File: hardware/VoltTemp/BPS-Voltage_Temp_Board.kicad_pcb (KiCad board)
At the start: 2 copper layers, 98.2 x 56.2 mm, 144 parts, among them IC1 ISO1641BDR, J10 53307-2471, J11 Conn_01x07, J12 Conn_01x04, J13 Conn_01x04, J5 Logic_Analyzer, J6 Conn_01x04, J7 Conn_01x04, J8 Conn_01x06, J9 Conn_01x03, SW1 BOOT, U1 EL3H7, U12 TLV9062xD, U13 TLV9062xD, U14 TLV9062xD, U2 BQ7692003PW, U3 EL3H7, U4 TLV9062xD, U6 TLV9062xD

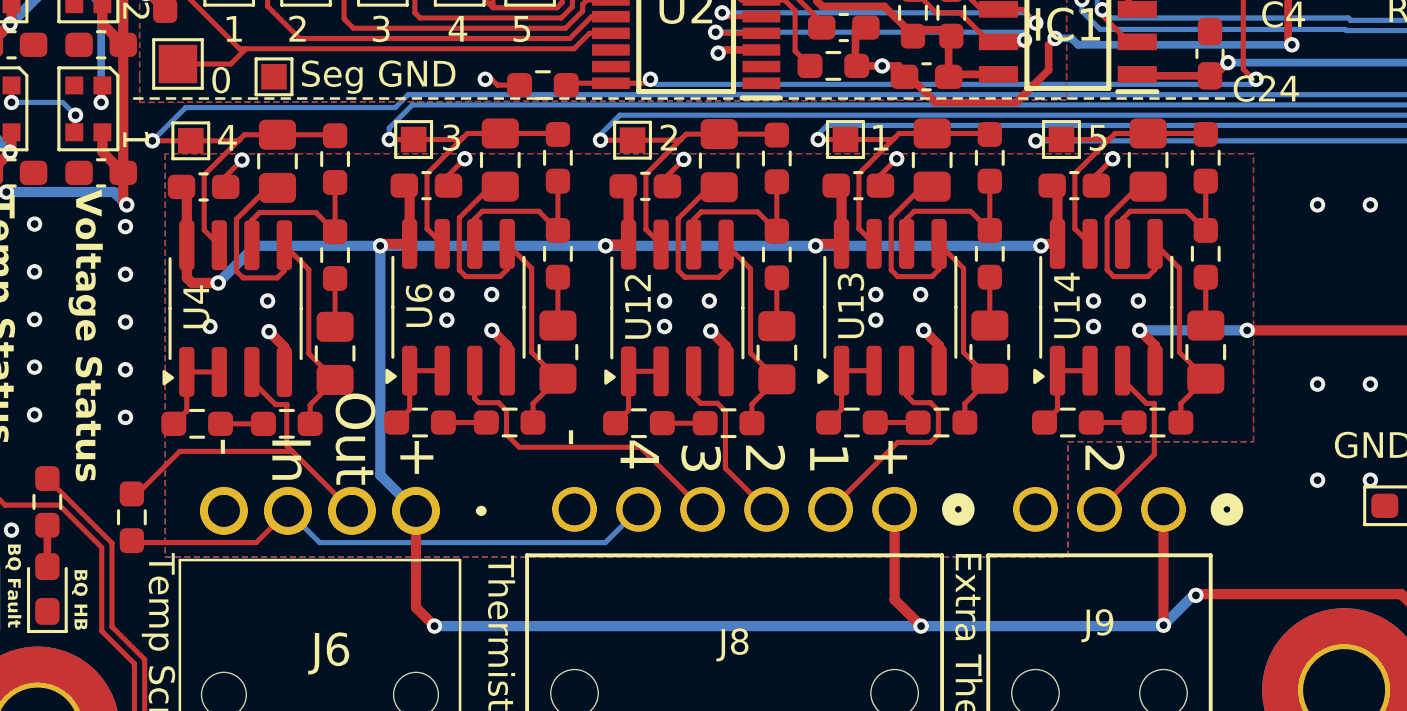
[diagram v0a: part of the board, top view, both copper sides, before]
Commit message: change 4.7pF cap to 470pF
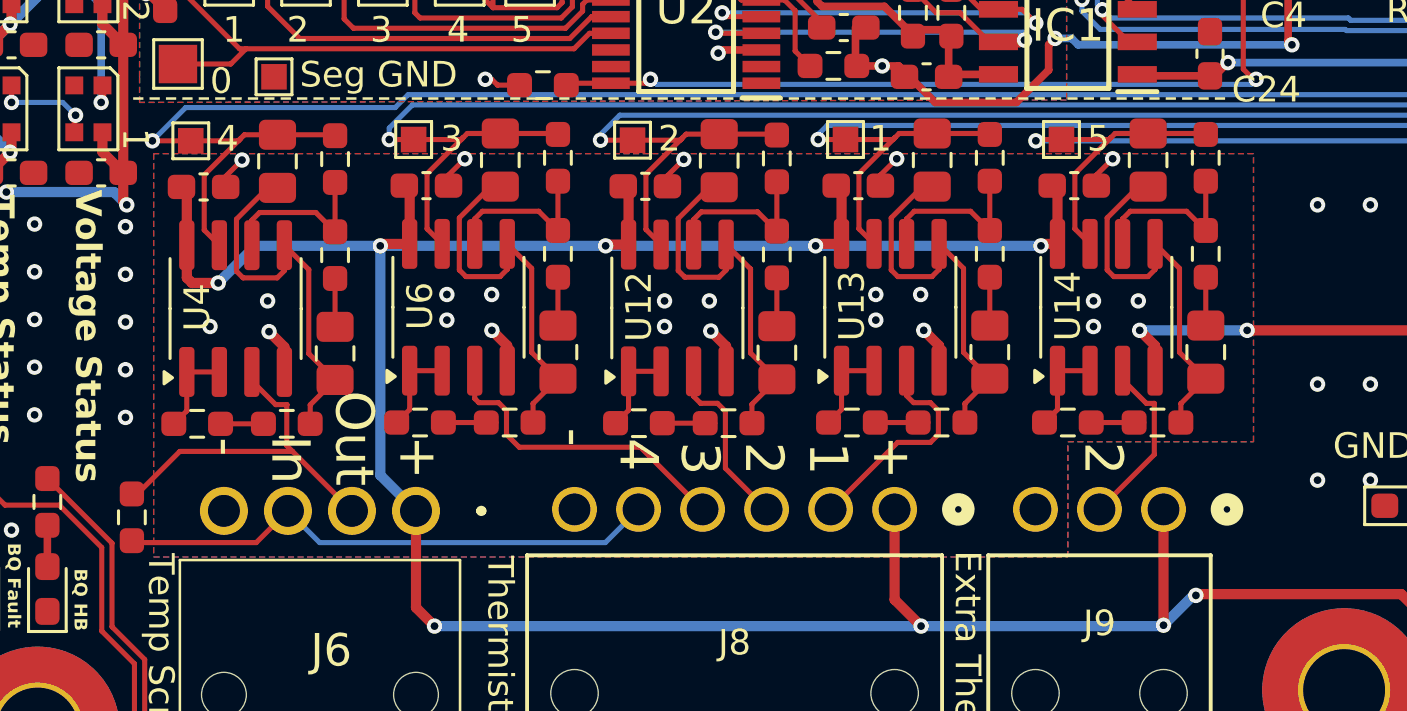
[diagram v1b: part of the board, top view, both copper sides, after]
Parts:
- C4: value 4.7pF -> 470pF
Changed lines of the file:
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@@
 			)
 		)
-		(property "Value" "4.7pF"
+		(property "Value" "470pF"
 			(at 0 1.43 90)
 			(layer "F.Fab")
@@
 			)
 		)
-		(property "P/N" "C0603C479J5GACAUTO"
+		(property "P/N" "06033C471K4Z2A"
 			(at 0 0 270)
 			(unlocked yes)
@@
 		(polygon
 			(pts
-				(xy 162.25 111.75) (xy 162.25 107.25) (xy 169.5 107.25) (xy 169.5 96) (xy 127 96) (xy 127 111.75)
+				(xy 162.25 111.75) (xy 162.25 107.25) (xy 169.5 107.25) (xy 169.5 96) (xy 126.55 96) (xy 126.55 111.75)
 			)
 		)

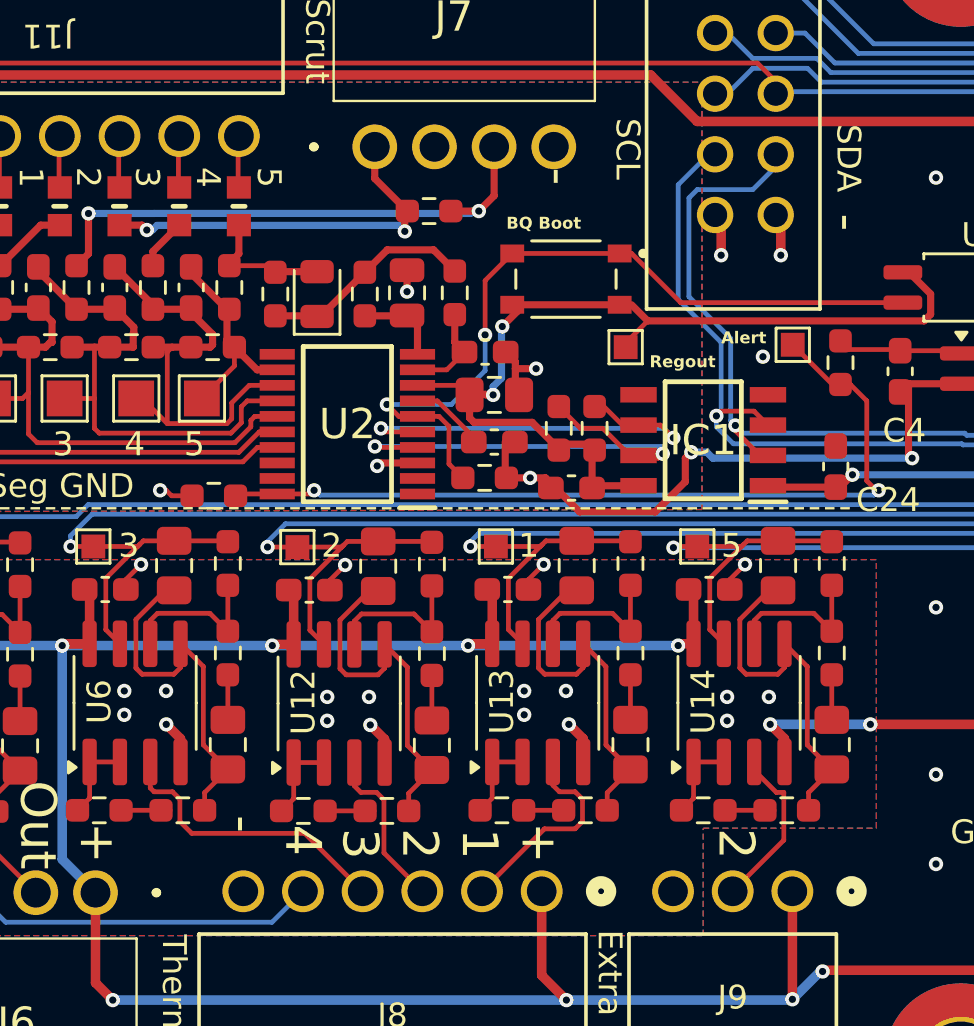
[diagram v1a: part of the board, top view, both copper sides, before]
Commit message: update connector silkscreen
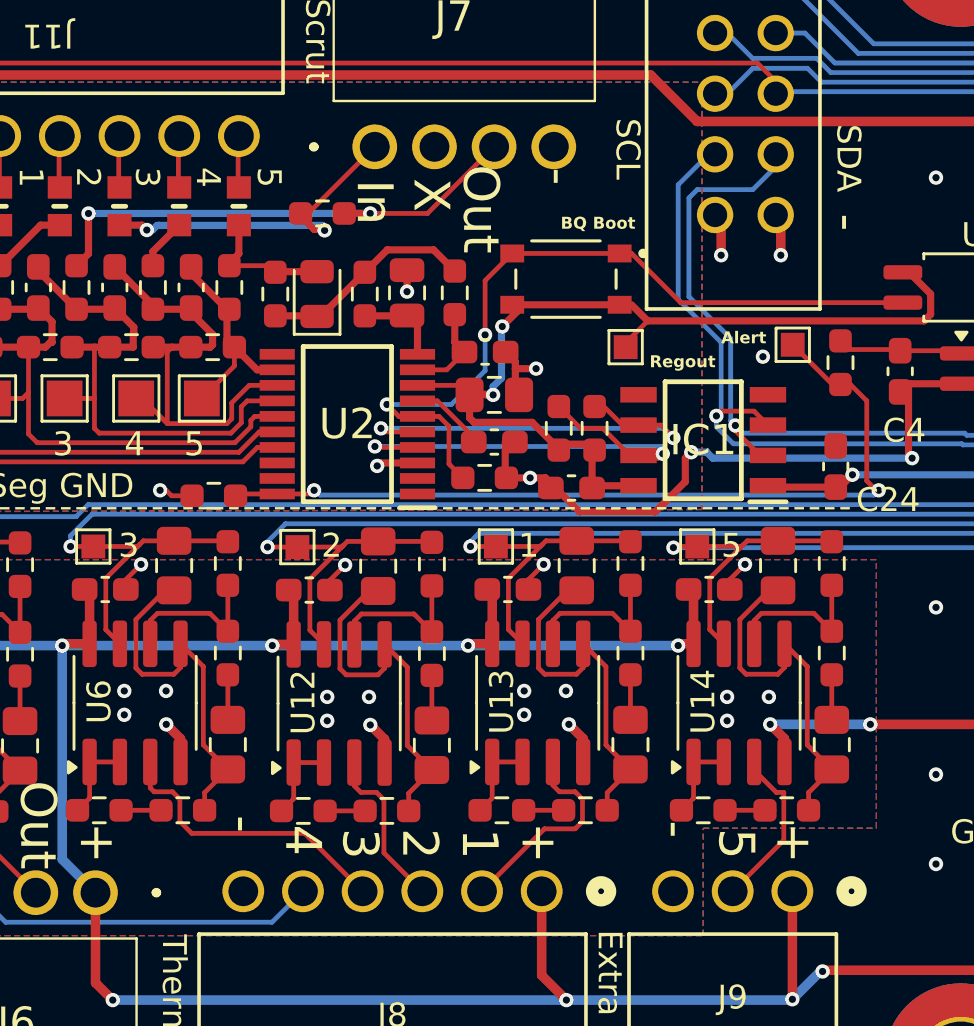
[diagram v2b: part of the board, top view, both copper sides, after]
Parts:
- moved R23 4.47 mm to (146.3, 81.5)
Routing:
- net /VoltageConn/3&4COM: track 16.4 -> 14.5 mm
- net /VoltageConn/3&4COM_Out: track 22.9 -> 21.7 mm
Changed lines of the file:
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@@
 	(footprint "Resistor_SMD:R_0603_1608Metric_Pad0.98x0.95mm_HandSolder"
 		(layer "F.Cu")
-		(at 150.7676 81.4)
+		(at 146.3 81.5)
 		(descr "Resistor SMD 0603 (1608 Metric), square (rectangular) end terminal, IPC_7351 nominal with elongated pad for handsoldering. (Body size source: IPC-SM-782 page 72, https://www.pcb-3d.com/wordpress/wp-content/uploads/ipc-sm-782a_amendment_1_and_2.pdf), generated with kicad-footprint-generator")
 		(tags "resistor handsolder")
@@
 	)
 	(gr_text "BQ Boot"
-		(at 154 82.2 0)
+		(at 156.275 82.2 0)
 		(layer "F.SilkS" knockout)
 		(effects
@@
 		)
 	)
+	(gr_text "In"
+		(at 147.6 80.075 270)
+		(layer "F.SilkS")
+		(effects
+			(font
+				(size 1.5 1.5)
+				(thickness 0.1)
+			)
+			(justify left bottom)
+		)
+	)
 	(gr_text "+"
 		(at 136 107 270)
@@
 		)
 	)
+	(gr_text "+"
+		(at 165.175 107 270)
+		(layer "F.SilkS")
+		(effects
+			(font
+				(size 1.5 1.5)
+				(thickness 0.1)
+			)
+			(justify left bottom)
+		)
+	)
 	(gr_text "5"
 		(at 140.5 91.75 0)
@@
 		)
 	)
-	(gr_text "2"
+	(gr_text "5"
 		(at 162.75 107.25 270)
 		(layer "F.SilkS")
@@
 		)
 	)
+	(gr_text "X"
+		(at 149.975 80.025 270)
+		(layer "F.SilkS")
+		(effects
+			(font
+				(size 1.5 1.5)
+				(thickness 0.1)
+			)
+			(justify left bottom)
+		)
+	)
+	(gr_text "-"
+		(at 160.225 106.925 270)
+		(layer "F.SilkS")
+		(effects
+			(font
+				(size 1.5 1.5)
+				(thickness 0.1)
+			)
+			(justify left bottom)
+		)
+	)
 	(gr_text "SDA"
 		(at 167.75 77.75 270)
@@
 		)
 	)
+	(gr_text "Out"
+		(at 152.05 79.45 270)
+		(layer "F.SilkS")
+		(effects
+			(font
+				(size 1.5 1.5)
+				(thickness 0.1)
+			)
+			(justify left bottom)
+		)
+	)
 	(gr_text "Extra Therm"
 		(at 157.75 111.5 270)
@@
 	)
 	(segment
+		(start 145.956097 82.168597)
+		(end 145.3875 81.6)
+		(width 0.3)
+		(layer "F.Cu")
+		(net 56)
+	)
+	(segment
 		(start 138.74 81.99)
 		(end 137.8 81.99)
@@
 	)
 	(segment
-		(start 148.491 78.708606)
-		(end 148.491 80.0359)
+		(start 146.351167 82.168597)
+		(end 145.956097 82.168597)
 		(width 0.3)
 		(layer "F.Cu")
@@
 	)
 	(segment
-		(start 148.491 80.0359)
-		(end 149.8551 81.4)
-		(width 0.3)
+		(start 145.3875 81.6)
+		(end 145.599606 81.6)
+		(width 0.2)
 		(layer "F.Cu")
 		(net 56)
 	)
 	(segment
-		(start 149.75 81.5051)
-		(end 149.8551 81.4)
-		(width 0.3)
+		(start 145.599606 81.6)
+		(end 148.491 78.708606)
+		(width 0.2)
 		(layer "F.Cu")
 		(net 56)
 	)
 	(segment
-		(start 149.75 82.25)
-		(end 149.75 81.5051)
+		(start 146.391194 82.208624)
+		(end 146.351167 82.168597)
 		(width 0.3)
 		(layer "F.Cu")
@@
 	)
 	(via
-		(at 149.75 82.25)
+		(at 146.391194 82.208624)
 		(size 0.6)
 		(drill 0.3)
@@
 	)
 	(segment
-		(start 139.176921 82.193839)
-		(end 139.37076 82)
+		(start 146.299289 82.116719)
+		(end 146.299289 82)
 		(width 0.3)
 		(layer "B.Cu")
@@
 	)
 	(segment
-		(start 138.943839 82.193839)
+		(start 139.458521 82)
+		(end 139.45752 82.001)
+		(width 0.3)
+		(layer "B.Cu")
+		(net 56)
+	)
+	(segment
+		(start 146.391194 82.208624)
+		(end 146.299289 82.116719)
+		(width 0.3)
+		(layer "B.Cu")
+		(net 56)
+	)
+	(segment
+		(start 139.36976 82.001)
 		(end 139.176921 82.193839)
 		(width 0.3)
@@
 	)
 	(segment
-		(start 149.5 82)
-		(end 149.75 82.25)
+		(start 139.45852 82)
+		(end 139.458521 82)
 		(width 0.3)
 		(layer "B.Cu")
@@
 	)
 	(segment
-		(start 139.37076 82)
-		(end 149.5 82)
+		(start 146.299289 82)
+		(end 139.45852 82)
 		(width 0.3)
 		(layer "B.Cu")
@@
 	)
 	(segment
-		(start 153.491 78.708606)
-		(end 153.491 80.759)
+		(start 139.45752 82.001)
+		(end 139.36976 82.001)
 		(width 0.3)
+		(layer "B.Cu")
+		(net 56)
+	)
+	(segment
+		(start 139.176921 82.193839)
+		(end 138.943839 82.193839)
+		(width 0.3)
+		(layer "B.Cu")
+		(net 56)
+	)
+	(segment
+		(start 150.700606 81.499)
+		(end 148.3 81.499)
+		(width 0.2)
 		(layer "F.Cu")
 		(net 57)
 	)
 	(segment
-		(start 152.85 81.4)
-		(end 151.6801 81.4)
-		(width 0.3)
+		(start 153.491 78.708606)
+		(end 150.700606 81.499)
+		(width 0.2)
 		(layer "F.Cu")
 		(net 57)
@@
 	)
 	(segment
-		(start 153.491 80.759)
-		(end 152.85 81.4)
+		(start 148.3 81.499)
+		(end 147.3135 81.499)
+		(width 0.3)
+		(layer "F.Cu")
+		(net 57)
+	)
+	(segment
+		(start 147.3135 81.499)
+		(end 147.2125 81.6)
 		(width 0.3)
 		(layer "F.Cu")
@@
 	)
 	(via
-		(at 152.85 81.4)
+		(at 148.3 81.499)
 		(size 0.6)
 		(drill 0.3)
@@
 	)
 	(segment
-		(start 152.85 81.4)
-		(end 152.6 81.4)
-		(width 0.3)
-		(layer "B.Cu")
-		(net 57)
-	)
-	(segment
 		(start 139.251 81.499)
 		(end 139.25 81.5)
@@
 	)
 	(segment
-		(start 149.707521 81.499)
+		(start 148.3 81.499)
 		(end 139.251 81.499)
 		(width 0.3)
@@
 	)
 	(segment
-		(start 152.5 81.5)
-		(end 149.708521 81.5)
-		(width 0.3)
-		(layer "B.Cu")
-		(net 57)
-	)
-	(segment
 		(start 139.25 81.5)
 		(end 136.5 81.5)
 		(width 0.3)
 		(layer "B.Cu")
-		(net 57)
-	)
-	(segment
-		(start 149.70752 81.499)
-		(end 149.707521 81.499)
-		(width 0.3)
-		(layer "B.Cu")
-		(net 57)
-	)
-	(segment
-		(start 152.6 81.4)
-		(end 152.5 81.5)
-		(width 0.3)
-		(layer "B.Cu")
-		(net 57)
-	)
-	(segment
-		(start 149.708521 81.5)
-		(end 149.70752 81.499)
-		(width 0.3)
-		(layer "B.Cu")

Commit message: update cubemx
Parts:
- moved LOGO1 4.88 mm to (196.6, 85.6)
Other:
- board text added: "Lakshay Gupta & Clark Rucker"
- board text added: "PA11"
- board text added: "PA12"
- board text added: "Todo: - Layout :( [X] - Update constrains [X] - Mirror thermistor flex pinout [X] - Label voltage connector [X] - Fix iso i2c footprint [X] - Make proper edge cuts [X] - Add stitching vias [X] - Update pcb from schematic once schematic todo done [X] - Figure out edge to connector clearance for nanofits [] - Redo addressable led routing [X] - Verify 24V traces can handle 8 Volttemps of current [X]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"
- board text removed: "Todo: - Layout :( [X] - Update constrains [X] - Mirror thermistor flex pinout [X] - Label voltage connector [] - Fix iso i2c footprint [X] - Make proper edge cuts [X] - Add stitching vias [X] - Update pcb from schematic once schematic todo done [X] - Figure out edge to connector clearance for nanofits [] - Redo addressable led routing [X] - Verify 24V traces can handle 8 Volttemps of current [X] 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"
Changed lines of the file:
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@@
 			)
 		)
+		(property "P/N" "53307-2471"
+			(at 0 0 180)
+			(unlocked yes)
+			(layer "F.Fab")
+			(hide yes)
+			(effects
+				(font
+					(size 1 1)
+					(thickness 0.15)
+				)
+			)
+		)
 		(sheetname "/")
 		(sheetfile "BPS-Voltage_Temp_Board.kicad_sch")
@@
 	(footprint "UTSVT_Logos:Hallock_Image_Small"
 		(layer "B.Cu")
-		(at 196.581263 80.688871 180)
+		(at 196.631263 85.563871 180)
 		(property "Reference" "LOGO1"
 			(at 0 0 0)
@@
 		)
 	)
+	(gr_text "Lakshay Gupta & Clark Rucker"
+		(at 176.8 69.85 0)
+		(layer "F.SilkS")
+		(effects
+			(font
+				(size 1 1)
+				(thickness 0.1)
+			)
+			(justify left bottom)
+		)
+	)
 	(gr_text "5"
 		(at 143.475 79.55 270)
@@
 		)
 	)
-	(gr_text "Todo:\n- Layout :( [X]\n- Update constrains [X]\n- Mirror thermistor flex pinout [X]\n- Label voltage connector []\n- Fix iso i2c footprint [X]\n- Make proper edge cuts [X]\n- Add stitching vias [X]\n- Update pcb from schematic once schematic todo done [X]\n- Figure out edge to connector clearance for nanofits []\n- Redo addressable led routing [X]\n- Verify 24V traces can handle 8 Volttemps of current [X]\n- Make silkscreen labeling consistent (0 vs 1 index) [X]\n- Reorganize logic analzyer pins for better rounting [X]\n- Place testpoints (fuck) [X]"
+	(gr_text "PA11"
+		(at 119.175 110.95 270)
+		(layer "B.SilkS")
+		(effects
+			(font
+				(size 1 1)
+				(thickness 0.1)
+			)
+			(justify left bottom)
+		)
+	)
+	(gr_text "PA12"
+		(at 121.8 110.875 270)
+		(layer "B.SilkS")
+		(effects
+			(font
+				(size 1 1)
+				(thickness 0.1)
+			)
+			(justify left bottom)
+		)
+	)
+	(gr_text "Todo:\n- Layout :( [X]\n- Update constrains [X]\n- Mirror thermistor flex pinout [X]\n- Label voltage connector [X]\n- Fix iso i2c footprint [X]\n- Make proper edge cuts [X]\n- Add stitching vias [X]\n- Update pcb from schematic once schematic todo done [X]\n- Figure out edge to connector clearance for nanofits []\n- Redo addressable led routing [X]\n- Verify 24V traces can handle 8 Volttemps of current [X]\n- Make silkscreen labeling consistent (0 vs 1 index) [X]\n- Reorganize logic analzyer pins for better rounting [X]\n- Place testpoints (fuck) [X]"
 		(at 66.9 86.1 0)
 		(layer "Cmts.User")
